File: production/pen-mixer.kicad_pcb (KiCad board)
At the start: 4 copper layers, 11 x 42 mm, 28 parts, among them J1 USB-C 16P, J2 BAT, U1 ISP1807-LR, U2 LSM6DS3TR-C, U3 MCP73831T-2ACI/OT, U4 TPS7A0533PDBV

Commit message: hide component designators
Claude-Session: https://claude.ai/code/session_01RCYT2QSY7BVZDeTyE9KrC4
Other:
- board text added: "Pen-mixer v1"
- board text removed: "pen-mixer v1"

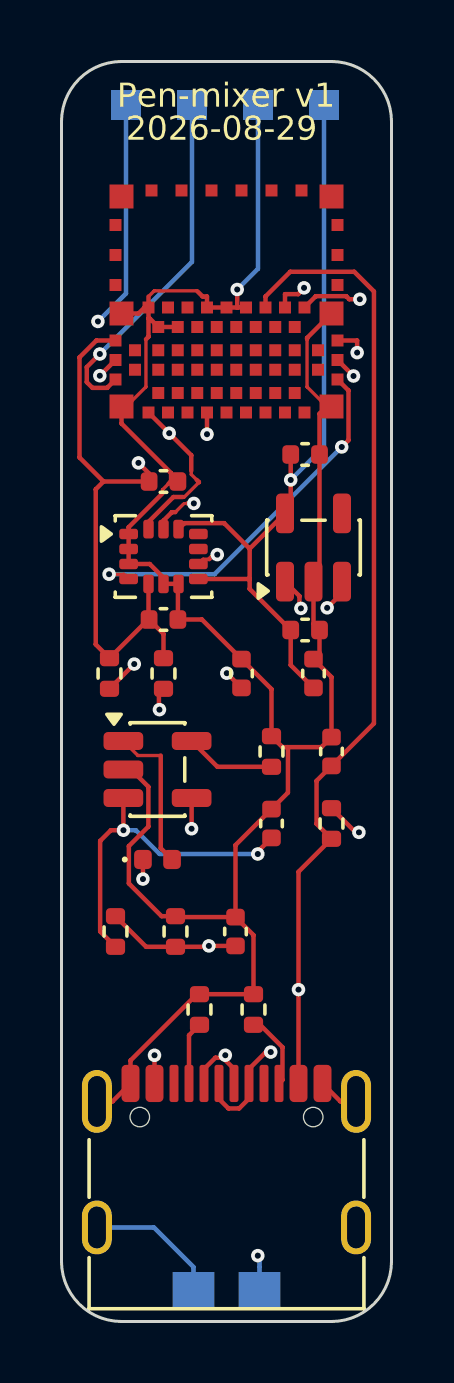
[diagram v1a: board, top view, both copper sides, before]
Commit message: add gnd copper zones
Claude-Session: https://claude.ai/code/session_01RCYT2QSY7BVZDeTyE9KrC4
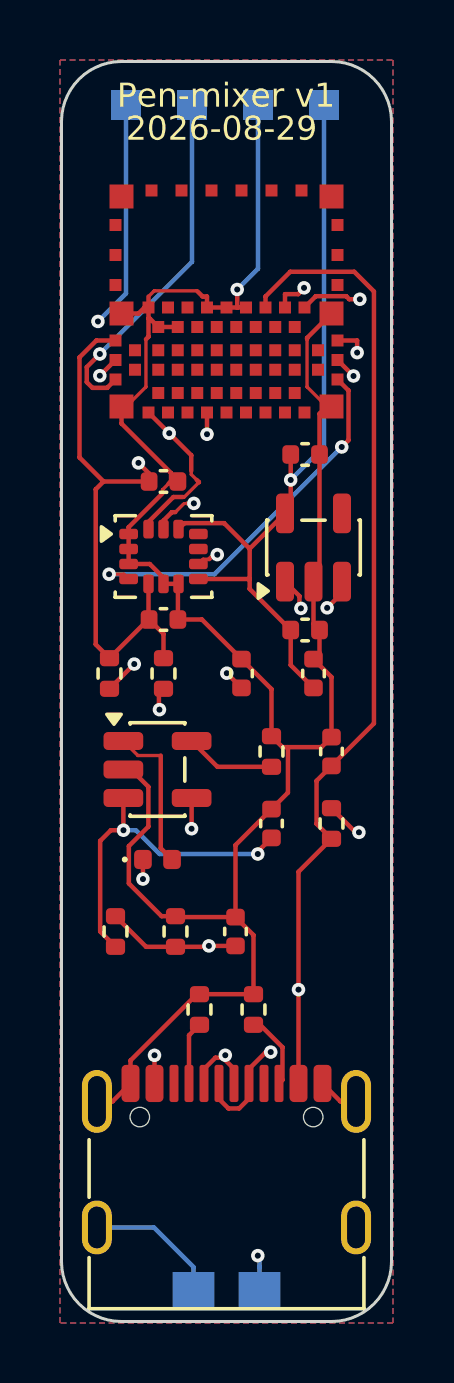
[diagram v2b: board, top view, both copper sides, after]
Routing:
- added copper zone on B.Cu, net GND
- added copper zone on F.Cu, net GND
- added copper zone on In1.Cu, net GND
- added copper zone on In2.Cu, net GND
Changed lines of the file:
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@@
 			(roundrect_rratio 0.25)
 			(net "GND")
+			(zone_connect 2)
 		)
 		(pad "B1" smd roundrect
@@
 			(roundrect_rratio 0.25)
 			(net "GND")
+			(zone_connect 2)
 		)
 		(pad "B4" smd roundrect
@@
 			(net "GND")
 			(solder_mask_margin 0.102)
+			(zone_connect 2)
 		)
 		(pad "8" smd rect
@@
 	)
 	(zone
+		(net "GND")
+		(layer "F.Cu")
+		(hatch edge 0.5)
+		(connect_pads
+			(clearance 0.2)
+		)
+		(min_thickness 0.2)
+		(fill yes
+			(thermal_gap 0.25)
+			(thermal_bridge_width 0.3)
+			(island_removal_mode 0)
+		)
+		(polygon
+			(pts
+				(xy 95.6952 42.4352) (xy 106.7952 42.4352) (xy 106.7952 84.5352) (xy 95.6952 84.5352)
+			)
+		)
+	)
+	(zone
 		(layers "F.Cu" "B.Cu" "In1.Cu" "In2.Cu")
 		(hatch edge 0.5)
@@
 			)
 		)
+	)
+	(zone
+		(net "GND")
+		(layer "B.Cu")
+		(hatch edge 0.5)
+		(connect_pads
+			(clearance 0.2)
+		)
+		(min_thickness 0.2)
+		(fill yes
+			(thermal_gap 0.25)
+			(thermal_bridge_width 0.3)
+			(island_removal_mode 0)
+		)
+		(polygon
+			(pts
+				(xy 95.6952 42.4352) (xy 106.7952 42.4352) (xy 106.7952 84.5352) (xy 95.6952 84.5352)
+			)
+		)
+	)
+	(zone
+		(net "GND")
+		(layer "In1.Cu")
+		(hatch edge 0.5)
+		(connect_pads
+			(clearance 0.2)
+		)
+		(min_thickness 0.2)
+		(fill yes
+			(thermal_gap 0.25)
+			(thermal_bridge_width 0.3)
+			(island_removal_mode 0)
+		)
+		(polygon
+			(pts
+				(xy 95.6952 42.4352) (xy 106.7952 42.4352) (xy 106.7952 84.5352) (xy 95.6952 84.5352)
+			)
+		)
+	)
+	(zone
+		(net "GND")
+		(layer "In2.Cu")
+		(hatch edge 0.5)
+		(connect_pads
+			(clearance 0.2)
+		)
+		(min_thickness 0.2)
+		(fill yes
+			(thermal_gap 0.25)
+			(thermal_bridge_width 0.3)
+			(island_removal_mode 0)
+		)
+		(polygon
+			(pts
+				(xy 95.6952 42.4352) (xy 106.7952 42.4352) (xy 106.7952 84.5352) (xy 95.6952 84.5352)
+			)
+		)
